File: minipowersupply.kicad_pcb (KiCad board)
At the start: 2 copper layers, 142.5 x 65.8 mm, 55 parts, among them J1 Conn_01x08_Female, J2 Conn_01x08_Female, J3 Conn_01x03_Female, J4 Conn_01x08_Female, J5 Conn_01x03_Female, J6 Conn_01x08_Female, J7 Conn_01x03_Female, J8 Conn_01x02_Female, J9 Conn_01x02_Female, Q1 BC817, U1 LM7805_TO220, U11 ACS70331EOLCTR-2P5U3, U13 ACS70331EOLCTR-2P5U3, U2 LM317L_TO92, U3 LM337L_TO92, U4 CD74HC4067SM, U5 ACS70331EOLCTR-2P5U3, U7 ACS70331EOLCTR-2P5U3, U9 ACS70331EOLCTR-2P5U3

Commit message: finalising diagram
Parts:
- removed C1, C2: 150uF, Capacitor_THT:CP_Radial_D8.0mm_P3.50mm
- removed C3, C4, C5, C6, C8: 100nF, Capacitor_THT:C_Disc_D8.0mm_W5.0mm_P5.00mm
- removed C7, C9: 1uF, Capacitor_THT:C_Disc_D8.0mm_W5.0mm_P5.00mm
- removed D1, D2, D3, D4, D5, D6: D, Diode_THT:D_T-1_P10.16mm_Horizontal
- removed F1: Fuse, Fuse:Fuseholder_Cylinder-5x20mm_Bulgin_FX0457_Horizontal_Closed
- removed J1, J2, J4, J6: Conn_01x08_Female, Connector_PinHeader_2.54mm:PinHeader_1x08_P2.54mm_Vertical
- removed J3, J5, J7: Conn_01x03_Female, Connector_PinHeader_2.54mm:PinHeader_1x03_P2.54mm_Vertical
- removed J8, J9: Conn_01x02_Female, Connector_PinHeader_2.54mm:PinHeader_1x02_P2.54mm_Vertical
- removed Q1: BC817, Package_TO_SOT_SMD:SOT-23
- removed R1: 410, Resistor_THT:R_Axial_DIN0207_L6.3mm_D2.5mm_P5.08mm_Vertical
- removed R10, R11, R14, R15, R16, R17, R20, R21, R6, R7: R_Small, Resistor_THT:R_Axial_DIN0207_L6.3mm_D2.5mm_P5.08mm_Vertical
- removed R2: 4.420k, Resistor_THT:R_Axial_DIN0207_L6.3mm_D2.5mm_P5.08mm_Vertical
- removed R3: 698, Resistor_THT:R_Axial_DIN0207_L6.3mm_D2.5mm_P5.08mm_Vertical
- removed TP1, TP2, TP3: TestPoint, TestPoint:TestPoint_THTPad_4.0x4.0mm_Drill2.0mm
- removed TR1: TRANSF3, minipowersupply:vtxtfr
- removed U1: LM7805_TO220, Package_TO_SOT_SMD:SOT-223-3_TabPin2
- removed U11, U13, U5, U7: ACS70331EOLCTR-2P5U3, ACS70331EOLCTR-2P5U3:SOIC127P600X175-8N
- removed U3: LM337L_TO92, Package_TO_SOT_THT:TO-92_Inline
- added R13: R_Small, Resistor_THT:R_Axial_DIN0207_L6.3mm_D2.5mm_P5.08mm_Vertical, F.Cu at (106.2, 53.9)
- added R18: R_Small, Resistor_THT:R_Axial_DIN0207_L6.3mm_D2.5mm_P5.08mm_Vertical, F.Cu at (58.6, 60.3)
- added R19: R_Small, Resistor_THT:R_Axial_DIN0207_L6.3mm_D2.5mm_P5.08mm_Vertical, F.Cu at (67.5, 53.9)
- added R22: R_Small, Resistor_THT:R_Axial_DIN0207_L6.3mm_D2.5mm_P5.08mm_Vertical, F.Cu at (202.1, 60.5)
- added R23: R_Small, Resistor_THT:R_Axial_DIN0207_L6.3mm_D2.5mm_P5.08mm_Vertical, F.Cu at (211.0, 54.1)
- added R8: R_Small, Resistor_THT:R_Axial_DIN0207_L6.3mm_D2.5mm_P5.08mm_Vertical, F.Cu at (124.8, 60.5)
- added R9: R_Small, Resistor_THT:R_Axial_DIN0207_L6.3mm_D2.5mm_P5.08mm_Vertical, F.Cu at (133.7, 54.1)
- added U12: ACS70331EOLCTR-2P5U3, ACS70331EOLCTR-2P5U3:SOIC127P600X175-8N, F.Cu at (61.3, 55.1)
- added U14: ACS70331EOLCTR-2P5U3, ACS70331EOLCTR-2P5U3:SOIC127P600X175-8N, F.Cu at (204.8, 55.3)
- added U6: ACS70331EOLCTR-2P5U3, ACS70331EOLCTR-2P5U3:SOIC127P600X175-8N, F.Cu at (100.0, 55.1)
- R4, R5: value 240 -> R_Small
- U2: value LM317L_TO92 -> ACS70331EOLCTR-2P5U3; footprint Package_TO_SOT_THT:TO-92_Inline -> ACS70331EOLCTR-2P5U3:SOIC127P600X175-8N
- U4: value CD74HC4067SM -> ACS70331EOLCTR-2P5U3; footprint Package_SO:SSOP-24_5.3x8.2mm_P0.65mm -> ACS70331EOLCTR-2P5U3:SOIC127P600X175-8N
- U9: value ACS70331EOLCTR-2P5U3 -> CD74HC4067SM; footprint ACS70331EOLCTR-2P5U3:SOIC127P600X175-8N -> Package_SO:SSOP-24_5.3x8.2mm_P0.65mm; moved to F.Cu
- moved U4 67.0 mm to (127.5, 55.3), turned to 0 degrees
- moved R5 60.3 mm to (172.4, 54.1)
- moved U2 56.0 mm to (166.2, 55.3), turned to 0 degrees
- moved R4 49.1 mm to (163.5, 60.5), turned to 0 degrees
- moved U9 39.8 mm to (135.0, 98.3), turned to 0 degrees
- moved A1 7.52 mm to (126.5, 115.8), turned to 0 degrees
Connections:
- A1 pad 4: /GND_0 -> /ArduinoMeasure/GND_0
- R4 pad 1: Net-(C7-Pad1) -> /ArduinoMeasure/Curent and Volt6/Out V
- R4 pad 2: Net-(J8-Pad2) -> /ArduinoMeasure/Curent and Volt6/Vsense
- R5 pad 1: Net-(C9-Pad2) -> /ArduinoMeasure/Curent and Volt6/Vsense
- R5 pad 2: Net-(J9-Pad2) -> /ArduinoMeasure/GND_0
- U2 pad 1: Net-(J8-Pad2) -> /ArduinoMeasure/Curent and Volt6/Out V
- U2 pad 2: Net-(C7-Pad1) -> /ArduinoMeasure/Curent and Volt6/Out V
- U2 pad 3: Net-(C6-Pad1) -> +5V
- U4 pad 1: Net-(A1-Pad20) -> /ArduinoMeasure/Curent and Volt7/Out V
- U4 pad 2: /Curent and Volt6/Vsense -> /ArduinoMeasure/Curent and Volt7/Out V
- U4 pad 3: /Curent and Volt6/Vinv -> /ArduinoMeasure/VA+
- U4 pad 4: /Curent and Volt5/Isense -> /ArduinoMeasure/VA+
- U4 pad 5: /Curent and Volt5/Vsense -> /ArduinoMeasure/GND_0
- U4 pad 6: /Curent and Volt5/Vinv -> unconnected-(U4-Pad6)
- U4 pad 7: /Curent and Volt4/Isense -> /ArduinoMeasure/Curent and Volt7/Isense
- U4 pad 8: /Curent and Volt4/Vsense -> +3.3V
- U9 pad 1: /Curent and Volt7/Out V -> Net-(A1-Pad20)
- U9 pad 2: /Curent and Volt7/Out V -> /ArduinoMeasure/Curent and Volt6/Vsense
- U9 pad 3: /VA+ -> /ArduinoMeasure/Curent and Volt6/Vinv
- U9 pad 4: /VA+ -> /ArduinoMeasure/Curent and Volt5/Isense
- U9 pad 5: /GND_0 -> /ArduinoMeasure/Curent and Volt5/Vsense
- U9 pad 6: unconnected-(U9-Pad6) -> /ArduinoMeasure/Curent and Volt5/Vinv
- U9 pad 7: /Curent and Volt7/Isense -> /ArduinoMeasure/Curent and Volt4/Isense
- U9 pad 8: +3.3V -> /ArduinoMeasure/Curent and Volt4/Vsense
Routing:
- net /V+: track 46.2 -> 0.00 mm
- net /V-: track 43.5 -> 0.00 mm
- net +5VA: track 31.8 -> 0.00 mm
- net /CK_0: track 29.7 -> 0.00 mm
- net Net-(TP2-Pad1): track 28.9 -> 0.00 mm
- net /VA-: track 28.1 -> 0.00 mm
- net Net-(C7-Pad1): track 27.8 -> 0.00 mm, vias 1 -> 0
- net Net-(D1-Pad2): track 26.7 -> 0.00 mm
- net Net-(D1-Pad1): track 24.9 -> 0.00 mm
- net Net-(D4-Pad1): track 24.3 -> 0.00 mm
- net Net-(C9-Pad2): track 23.3 -> 0.00 mm
- net +5V: track 21.5 -> 0.00 mm
- net Net-(J8-Pad2): track 21.2 -> 0.00 mm
- net /CK: track 20.9 -> 0.00 mm
- net /Curent and Volt7/Out V: track 19.4 -> 0.00 mm
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- removed copper zone on B.Cu, net /DUAL0V
- removed copper zone on F.Cu, net /DUAL0V
- removed copper zone on B.Cu, net /GND_0
- removed copper zone on F.Cu, net /GND_0
- removed copper zone on B.Cu, net /GND_REG
- removed copper zone on F.Cu, net /GND_REG
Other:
- board size 142.5 x 65.8 mm -> 109.5 x 61.2 mm

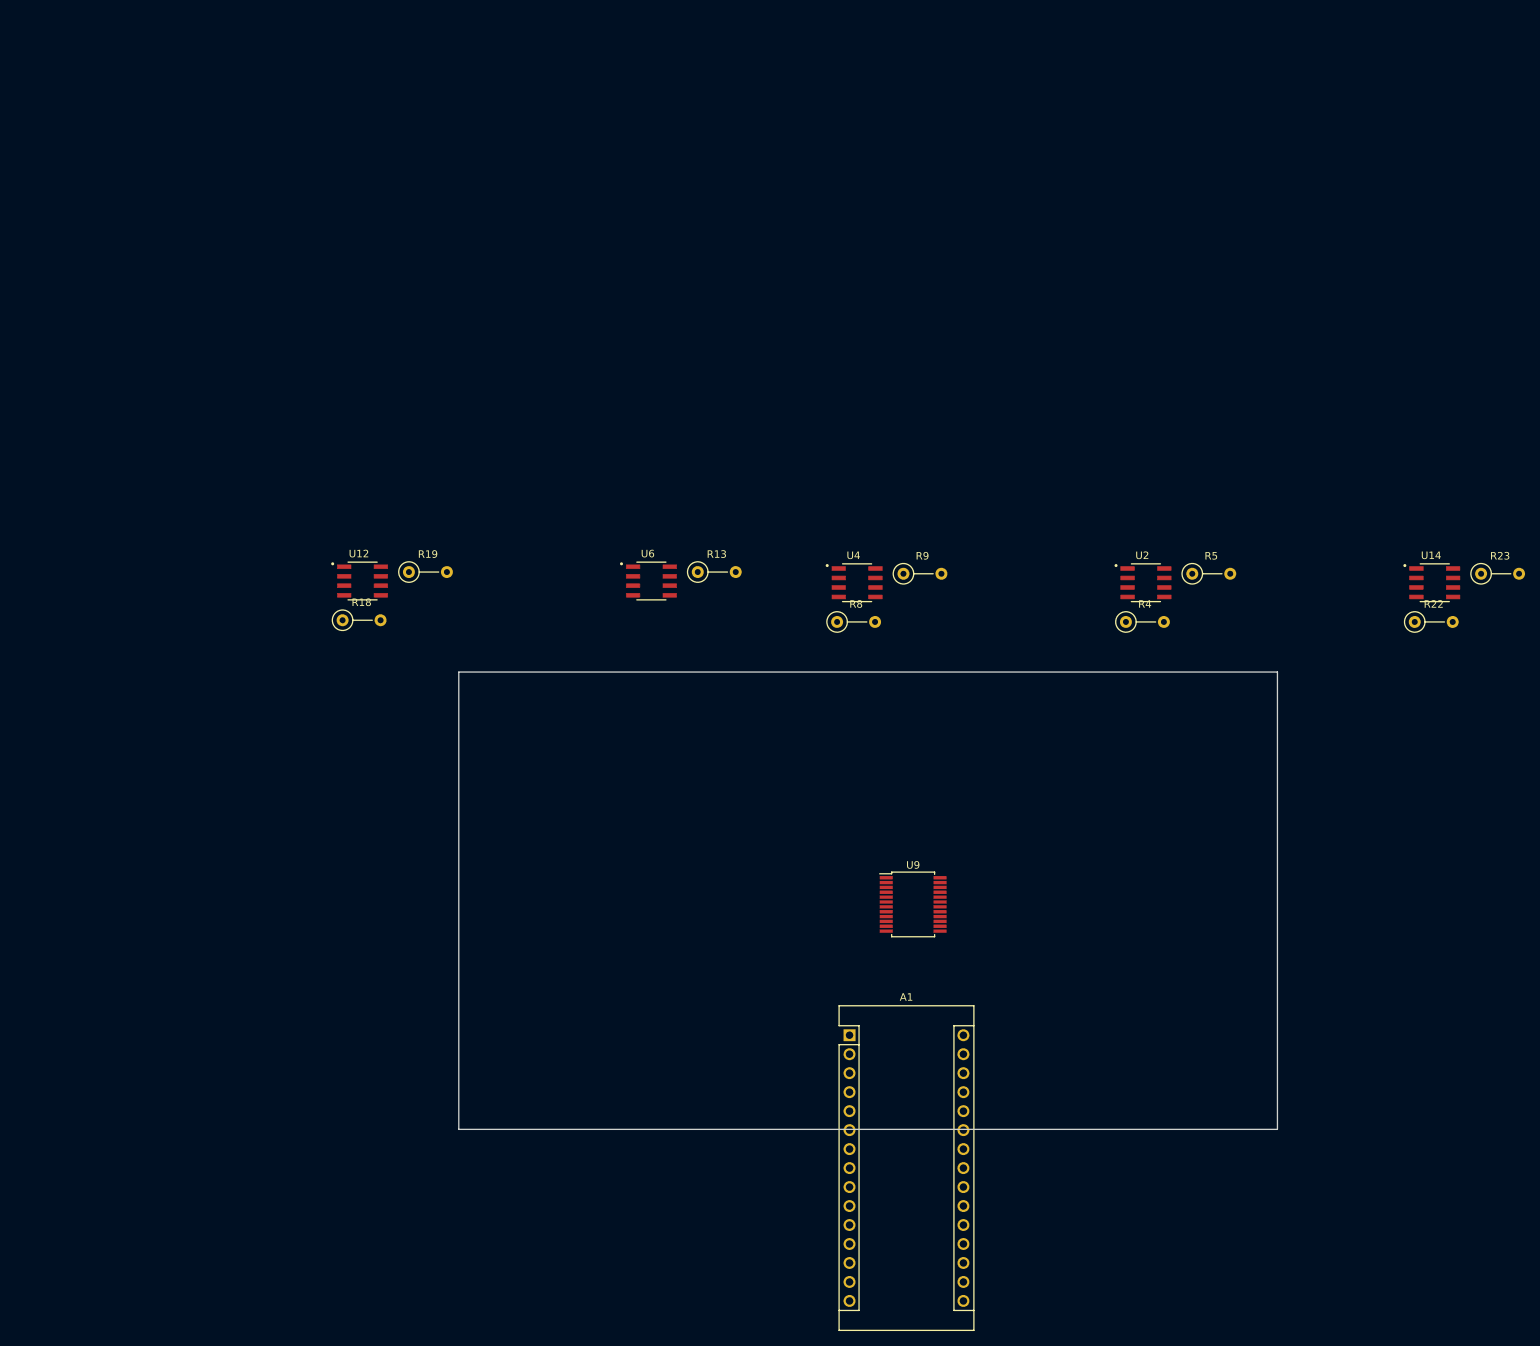
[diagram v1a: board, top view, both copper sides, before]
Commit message: sorting out earths and making measure mux board
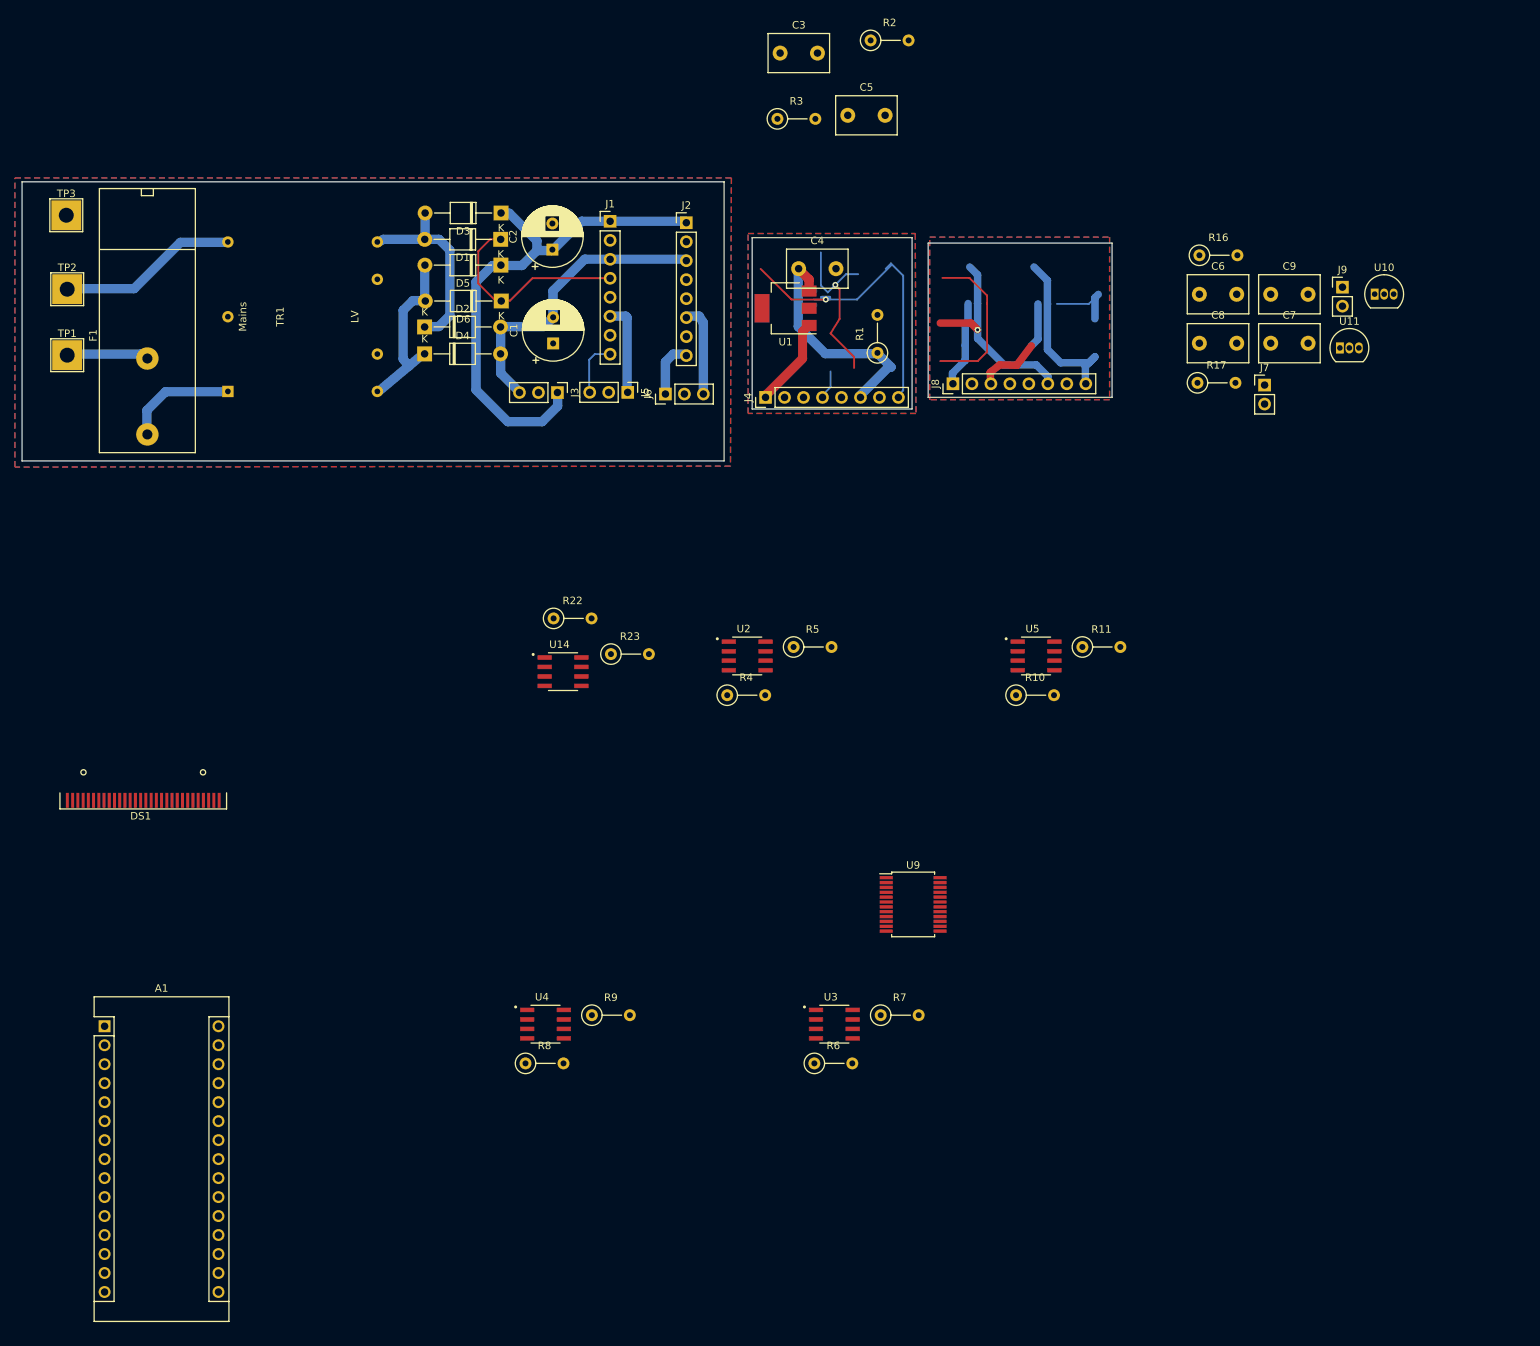
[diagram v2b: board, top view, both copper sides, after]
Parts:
- removed R13, R18, R19: R_Small, Resistor_THT:R_Axial_DIN0207_L6.3mm_D2.5mm_P5.08mm_Vertical
- removed U12, U6: ACS70331EOLCTR-2P5U3, ACS70331EOLCTR-2P5U3:SOIC127P600X175-8N
- added C1: 150uF, Capacitor_THT:CP_Radial_D8.0mm_P3.50mm, F.Cu at (86.8, 23.3)
- added C2: 150uF, Capacitor_THT:CP_Radial_D8.0mm_P3.50mm, F.Cu at (86.7, 10.7)
- added C3: 100nF, Capacitor_THT:C_Disc_D8.0mm_W5.0mm_P5.00mm, F.Cu at (117.2, -15.6)
- added C4: 100nF, Capacitor_THT:C_Disc_D8.0mm_W5.0mm_P5.00mm, F.Cu at (119.7, 13.3)
- added C5: 100nF, Capacitor_THT:C_Disc_D8.0mm_W5.0mm_P5.00mm, F.Cu at (126.2, -7.25)
- added C6: 100nF, Capacitor_THT:C_Disc_D8.0mm_W5.0mm_P5.00mm, F.Cu at (173.3, 16.7)
- added C7: 1uF, Capacitor_THT:C_Disc_D8.0mm_W5.0mm_P5.00mm, F.Cu at (182.8, 23.2)
- added C8: 100nF, Capacitor_THT:C_Disc_D8.0mm_W5.0mm_P5.00mm, F.Cu at (173.3, 23.2)
- added C9: 1uF, Capacitor_THT:C_Disc_D8.0mm_W5.0mm_P5.00mm, F.Cu at (182.8, 16.7)
- added D1: D, Diode_THT:D_T-1_P10.16mm_Horizontal, F.Cu at (79.8, 9.35)
- added D2: D, Diode_THT:D_T-1_P10.16mm_Horizontal, F.Cu at (69.6, 21.1)
- added D3: D, Diode_THT:D_T-1_P10.16mm_Horizontal, F.Cu at (79.9, 5.83)
- added D4: D, Diode_THT:D_T-1_P10.16mm_Horizontal, F.Cu at (69.6, 24.7)
- added D5: D, Diode_THT:D_T-1_P10.16mm_Horizontal, F.Cu at (79.8, 12.8)
- added D6: D, Diode_THT:D_T-1_P10.16mm_Horizontal, F.Cu at (79.9, 17.6)
- added DS1: OLED-128O064D, Display:OLED-128O064D, F.Cu at (32.0, 84.4)
- added F1: Fuse, Fuse:Fuseholder_Cylinder-5x20mm_Bulgin_FX0457_Horizontal_Closed, F.Cu at (32.5, 35.5)
- added J1: Conn_01x08_Female, Connector_PinHeader_2.54mm:PinHeader_1x08_P2.54mm_Vertical, F.Cu at (94.5, 6.94)
- added J2: Conn_01x08_Female, Connector_PinHeader_2.54mm:PinHeader_1x08_P2.54mm_Vertical, F.Cu at (104.7, 7.12)
- added J3: Conn_01x03_Female, Connector_PinHeader_2.54mm:PinHeader_1x03_P2.54mm_Vertical, F.Cu at (87.4, 29.9)
- added J4: Conn_01x08_Female, Connector_PinHeader_2.54mm:PinHeader_1x08_P2.54mm_Vertical, F.Cu at (115.2, 30.5)
- added J5: Conn_01x03_Female, Connector_PinHeader_2.54mm:PinHeader_1x03_P2.54mm_Vertical, F.Cu at (96.8, 29.8)
- added J6: Conn_01x03_Female, Connector_PinHeader_2.54mm:PinHeader_1x03_P2.54mm_Vertical, F.Cu at (101.8, 30.1)
- added J7: Conn_01x02_Female, Connector_PinHeader_2.54mm:PinHeader_1x02_P2.54mm_Vertical, F.Cu at (182.0, 28.9)
- added J8: Conn_01x08_Female, Connector_PinHeader_2.54mm:PinHeader_1x08_P2.54mm_Vertical, F.Cu at (140.3, 28.7)
- added J9: Conn_01x02_Female, Connector_PinHeader_2.54mm:PinHeader_1x02_P2.54mm_Vertical, F.Cu at (192.4, 15.8)
- added Q1: BC817, Package_TO_SOT_SMD:SOT-23, B.Cu at (122.3, 17.2)
- added R1: 410, Resistor_THT:R_Axial_DIN0207_L6.3mm_D2.5mm_P5.08mm_Vertical, F.Cu at (130.2, 24.5)
- added R10: R_Small, Resistor_THT:R_Axial_DIN0207_L6.3mm_D2.5mm_P5.08mm_Vertical, F.Cu at (148.8, 70.3)
- added R11: R_Small, Resistor_THT:R_Axial_DIN0207_L6.3mm_D2.5mm_P5.08mm_Vertical, F.Cu at (157.7, 63.9)
- added R16: 240, Resistor_THT:R_Axial_DIN0207_L6.3mm_D2.5mm_P5.08mm_Vertical, F.Cu at (173.3, 11.5)
- added R17: 240, Resistor_THT:R_Axial_DIN0207_L6.3mm_D2.5mm_P5.08mm_Vertical, F.Cu at (173.1, 28.6)
- added R2: 4.420k, Resistor_THT:R_Axial_DIN0207_L6.3mm_D2.5mm_P5.08mm_Vertical, F.Cu at (129.3, -17.3)
- added R3: 698, Resistor_THT:R_Axial_DIN0207_L6.3mm_D2.5mm_P5.08mm_Vertical, F.Cu at (116.8, -6.78)
- added R6: R_Small, Resistor_THT:R_Axial_DIN0207_L6.3mm_D2.5mm_P5.08mm_Vertical, F.Cu at (121.8, 119.6)
- added R7: R_Small, Resistor_THT:R_Axial_DIN0207_L6.3mm_D2.5mm_P5.08mm_Vertical, F.Cu at (130.7, 113.2)
- added TP1: TestPoint, TestPoint:TestPoint_THTPad_4.0x4.0mm_Drill2.0mm, F.Cu at (21.8, 24.9)
- added TP2: TestPoint, TestPoint:TestPoint_THTPad_4.0x4.0mm_Drill2.0mm, F.Cu at (21.8, 16.0)
- added TP3: TestPoint, TestPoint:TestPoint_THTPad_4.0x4.0mm_Drill2.0mm, F.Cu at (21.7, 6.12)
- added TR1: TRANSF3, minipowersupply:vtxtfr, F.Cu at (53.3, 19.7)
- added U1: LM7805_TO220, Package_TO_SOT_SMD:SOT-223-3_TabPin2, F.Cu at (117.9, 18.6)
- added U10: LM317L_TO92, Package_TO_SOT_THT:TO-92_Inline, F.Cu at (196.8, 16.7)
- added U11: LM337L_TO92, Package_TO_SOT_THT:TO-92_Inline, F.Cu at (192.1, 23.9)
- added U3: ACS70331EOLCTR-2P5U3, ACS70331EOLCTR-2P5U3:SOIC127P600X175-8N, F.Cu at (124.5, 114.4)
- added U5: ACS70331EOLCTR-2P5U3, ACS70331EOLCTR-2P5U3:SOIC127P600X175-8N, F.Cu at (151.4, 65.1)
- moved U14 117.3 mm to (88.2, 67.2)
- moved R23 116.9 mm to (94.6, 64.8)
- moved R22 115.2 mm to (86.9, 60.1)
- moved A1 99.7 mm to (26.8, 114.7)
- moved R9 72.3 mm to (92.0, 113.2)
- moved R8 72.3 mm to (83.1, 119.6)
- moved U4 72.3 mm to (85.8, 114.4)
- moved U2 54.2 mm to (112.8, 65.1)
- moved R4 54.2 mm to (110.1, 70.3)
- moved R5 54.2 mm to (119.0, 63.9)
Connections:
- net /ArduinoMeasure/Curent and Volt4/Out V renamed / Measure and Mux/Curent and Volt4/Out V
- net /ArduinoMeasure/Curent and Volt6/Out V renamed / Measure and Mux/Curent and Volt5/Out V
- net /ArduinoMeasure/Curent and Volt7/Out V renamed / Measure and Mux/Curent and Volt7/Out V
- net /ArduinoMeasure/VA+ renamed / Measure and Mux/Curent and Volt7/Vin
- A1 pad 10: unconnected-(A1-Pad10) -> / Measure and Mux/A3
- A1 pad 11: unconnected-(A1-Pad11) -> / Measure and Mux/A2
- A1 pad 12: unconnected-(A1-Pad12) -> / Measure and Mux/A1
- A1 pad 13: Net-(A1-Pad13) -> / Measure and Mux/A0
- A1 pad 14: Net-(A1-Pad14) -> / Measure and Mux/EN
- A1 pad 15: Net-(A1-Pad15) -> unconnected-(A1-Pad15)
- A1 pad 16: Net-(A1-Pad16) -> unconnected-(A1-Pad16)
- A1 pad 17: unconnected-(A1-Pad17) -> / Measure and Mux/3v3
- A1 pad 19: unconnected-(A1-Pad19) -> Net-(A1-Pad19)
- A1 pad 27: +5V -> / Measure and Mux/V5+
- A1 pad 29: unconnected-(A1-Pad29) -> GNDREF
- A1 pad 30: unconnected-(A1-Pad30) -> / Measure and Mux/Vunreg+
- A1 pad 4: /ArduinoMeasure/GND_0 -> GNDREF
- R22 pad 2: /ArduinoMeasure/Curent and Volt4/Vsense -> / Measure and Mux/Curent and Volt4/Vsense
- R23 pad 1: /ArduinoMeasure/Curent and Volt4/Vsense -> / Measure and Mux/Curent and Volt4/Vsense
- R23 pad 2: /ArduinoMeasure/GND_0 -> / Measure and Mux/Curent and Volt4/GND
- R4 pad 2: /ArduinoMeasure/Curent and Volt6/Vsense -> / Measure and Mux/Curent and Volt5/Vsense
- R5 pad 1: /ArduinoMeasure/Curent and Volt6/Vsense -> / Measure and Mux/Curent and Volt5/Vsense
- R5 pad 2: /ArduinoMeasure/GND_0 -> / Measure and Mux/Curent and Volt4/GND
- R8 pad 2: /ArduinoMeasure/Curent and Volt7/Vsense -> / Measure and Mux/Curent and Volt7/Vsense
- R9 pad 1: /ArduinoMeasure/Curent and Volt7/Vsense -> / Measure and Mux/Curent and Volt7/Vsense
- R9 pad 2: /ArduinoMeasure/GND_0 -> / Measure and Mux/Curent and Volt4/GND
- U14 pad 3: /ArduinoMeasure/V+ -> / Measure and Mux/Vunreg+
- U14 pad 4: /ArduinoMeasure/V+ -> / Measure and Mux/Vunreg+
- U14 pad 5: /ArduinoMeasure/GND_0 -> / Measure and Mux/Curent and Volt4/GND
- U14 pad 7: /ArduinoMeasure/Curent and Volt4/Isense -> / Measure and Mux/Curent and Volt4/Isense
- U14 pad 8: +3.3V -> / Measure and Mux/3v3
- U2 pad 3: +5V -> / Measure and Mux/Vunreg-
- U2 pad 4: +5V -> / Measure and Mux/Vunreg-
- U2 pad 5: /ArduinoMeasure/GND_0 -> / Measure and Mux/Curent and Volt4/GND
- U2 pad 7: /ArduinoMeasure/Curent and Volt6/Isense -> / Measure and Mux/Curent and Volt5/Isense
- U2 pad 8: +3.3V -> / Measure and Mux/3v3
- U4 pad 5: /ArduinoMeasure/GND_0 -> / Measure and Mux/Curent and Volt4/GND
- U4 pad 7: /ArduinoMeasure/Curent and Volt7/Isense -> / Measure and Mux/Curent and Volt7/Isense
- U4 pad 8: +3.3V -> / Measure and Mux/3v3
- U9 pad 1: Net-(A1-Pad20) -> / Measure and Mux/Aout
- U9 pad 10: Net-(A1-Pad16) -> / Measure and Mux/A0
- U9 pad 11: Net-(A1-Pad15) -> / Measure and Mux/A1
- U9 pad 12: /ArduinoMeasure/GND_0 -> / Measure and Mux/Curent and Volt4/GND
- U9 pad 13: Net-(A1-Pad13) -> / Measure and Mux/A3
- U9 pad 14: Net-(A1-Pad14) -> / Measure and Mux/A2
- U9 pad 15: /ArduinoMeasure/GND_0 -> / Measure and Mux/EN
- U9 pad 17: /ArduinoMeasure/Curent and Volt8/Isense -> unconnected-(U9-Pad17)
- U9 pad 18: /ArduinoMeasure/Curent and Volt8/Vsense -> unconnected-(U9-Pad18)
- U9 pad 19: /ArduinoMeasure/Curent and Volt8/Vinv -> unconnected-(U9-Pad19)
- U9 pad 2: /ArduinoMeasure/Curent and Volt6/Vsense -> / Measure and Mux/Curent and Volt7/Isense
- U9 pad 20: /ArduinoMeasure/Curent and Volt7/Isense -> unconnected-(U9-Pad20)
- U9 pad 21: /ArduinoMeasure/Curent and Volt7/Vsense -> unconnected-(U9-Pad21)
- U9 pad 22: /ArduinoMeasure/Curent and Volt7/Vinv -> / Measure and Mux/Curent and Volt8/Isense
- U9 pad 23: /ArduinoMeasure/Curent and Volt6/Isense -> / Measure and Mux/Curent and Volt8/Vsense
- U9 pad 24: +5V -> / Measure and Mux/V5+
- U9 pad 3: /ArduinoMeasure/Curent and Volt6/Vinv -> / Measure and Mux/Curent and Volt7/Vsense
- U9 pad 4: /ArduinoMeasure/Curent and Volt5/Isense -> / Measure and Mux/Curent and Volt6/Isense
- U9 pad 5: /ArduinoMeasure/Curent and Volt5/Vsense -> / Measure and Mux/Curent and Volt6/Vsense
- U9 pad 6: /ArduinoMeasure/Curent and Volt5/Vinv -> / Measure and Mux/Curent and Volt5/Isense
- U9 pad 7: /ArduinoMeasure/Curent and Volt4/Isense -> / Measure and Mux/Curent and Volt5/Vsense
- U9 pad 8: /ArduinoMeasure/Curent and Volt4/Vsense -> / Measure and Mux/Curent and Volt4/Isense
- U9 pad 9: /ArduinoMeasure/Curent and Volt4/Vinv -> / Measure and Mux/Curent and Volt4/Vsense
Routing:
- net /Unregulated Power/V+: track 0.00 -> 69.1 mm
- net /Clock and TTL/CK: track 0.00 -> 42.1 mm, vias 0 -> 1
- net /Unregulated Power/V-: track 0.00 -> 40.5 mm
- net (no net): track 0.00 -> 36.7 mm
- net +5VA: track 0.00 -> 31.6 mm
- net Net-(C7-Pad1): track 0.00 -> 27.8 mm, vias 0 -> 1
- net Net-(D1-Pad1): track 0.00 -> 27.6 mm
- net Net-(D1-Pad2): track 0.00 -> 26.5 mm
- net Net-(TP2-Pad1): track 0.00 -> 24.2 mm
- net Net-(D4-Pad1): track 0.00 -> 24.0 mm
- net Net-(D7-Pad2): track 0.00 -> 23.8 mm, vias 0 -> 1
- net Net-(C9-Pad2): track 0.00 -> 23.3 mm
- net Net-(F1-Pad1): track 0.00 -> 15.4 mm
- net Net-(J1-Pad6): track 0.00 -> 12.7 mm
- net Net-(J2-Pad6): track 0.00 -> 12.2 mm
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- added copper zone on B.Cu, net (none)
- added copper zone on F.Cu, net (none)
- added copper zone on B.Cu, net /Clock and TTL/GND_0
- added copper zone on F.Cu, net /Clock and TTL/GND_0
- added copper zone on B.Cu, net Earth
- added copper zone on F.Cu, net Earth
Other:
- board size 109.5 x 61.2 mm -> 145.9 x 37.4 mm
